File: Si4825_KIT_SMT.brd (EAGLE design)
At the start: 44.5 x 38.1 mm, 26 parts, among them U1 SI4825, U2 LMV358SOIC, Y1 32.768kHz

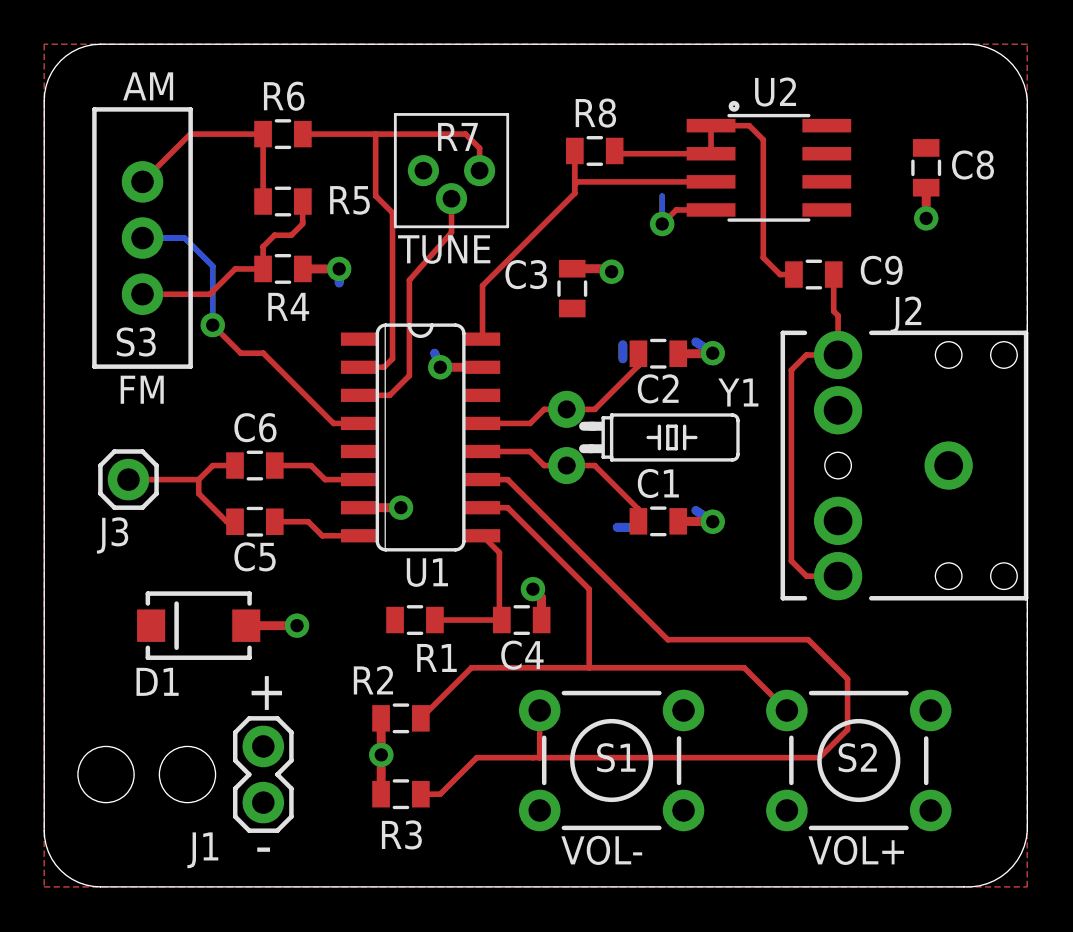
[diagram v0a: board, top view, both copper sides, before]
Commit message: Fixed issues discovered in first build
- fixed potentiometer footprint
- bigger strain relief holes: .1” to .15”
- changed value of C9 (AC coupling capacitor) to 22uF in BOM and
schematic
- Removed R8 (jumper to bypass op amp)
- Increased length of surface mount pads for 0805 components to
facilitate hand soldering
- Regenerated gerbers, jpg previews, and pdf of schematic
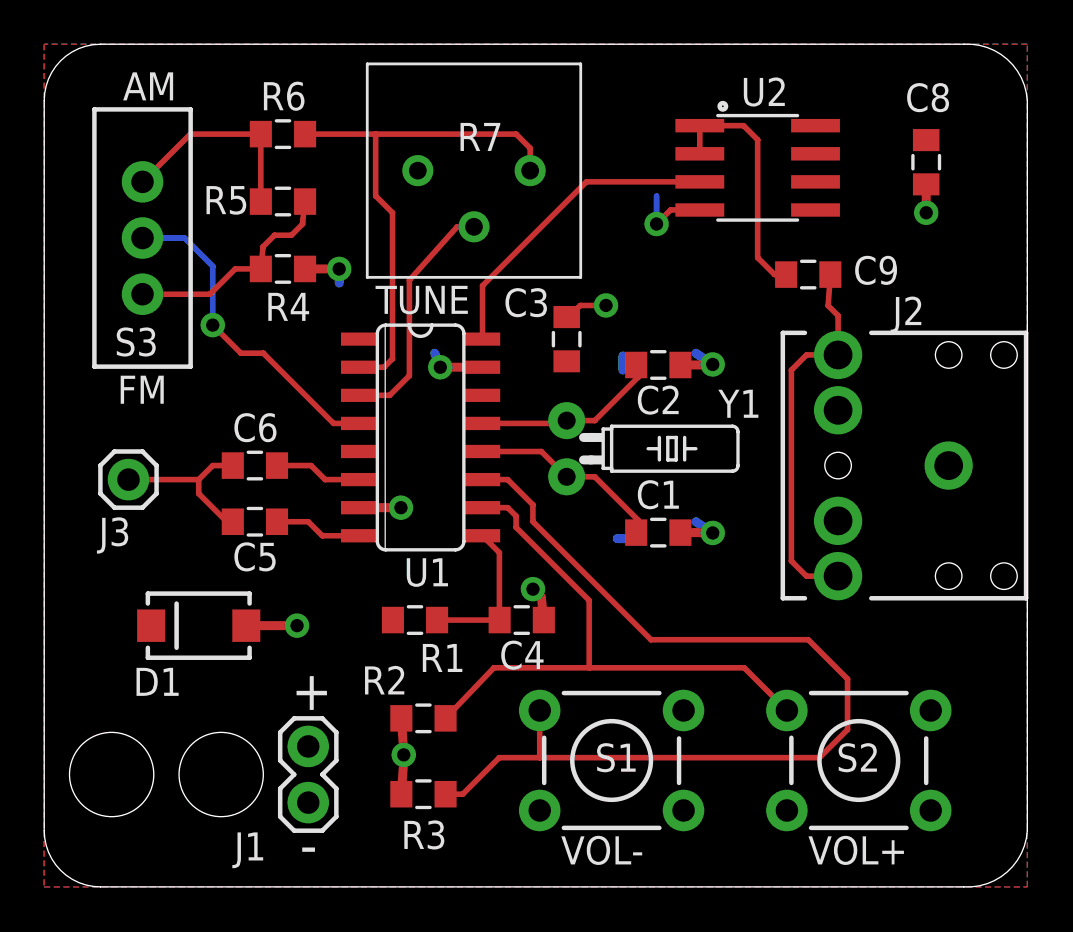
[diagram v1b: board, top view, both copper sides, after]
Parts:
- removed R8: 0, SparkFun-Resistors:0805
- C9: value 1uF -> 22uF
- moved C3 2.30 mm to (23.6, 24.8)
- moved J1 2.03 mm to (11.9, 3.81)
- moved R7 1.02 mm to (19.4, 32.4)
- moved R2 1.02 mm to (17.1, 7.62)
- moved R3 1.02 mm to (17.1, 4.19)
- moved C2 0.51 mm to (27.8, 23.6)
- moved C1 0.51 mm to (27.8, 16.0)
- moved Y1 0.51 mm to (23.6, 19.8)
- moved U2 0.51 mm to (32.3, 32.5)
- moved C9 0.25 mm to (34.5, 27.7)
- moved C8 0.25 mm to (39.9, 32.8)
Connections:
- net N$14: no longer R8.1
- net N$17: no longer R8.2
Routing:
- net N$17: track 15.4 -> 11.1 mm
- net N$14: track 16.4 -> 14.2 mm
- net N$10: track 21.4 -> 23.6 mm
- net N$5: track 28.2 -> 27.1 mm
- net N$6: track 45.2 -> 44.5 mm
- net GND: track 27.9 -> 27.4 mm
